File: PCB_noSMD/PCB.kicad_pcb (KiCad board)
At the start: 2 copper layers, 48.3 x 81.3 mm, 7 parts, among them J10 Screw_Terminal_01x02, J4 Conn_01x12_Socket, J5 Conn_01x16_Socket, J6 Conn_01x08_Socket, J7 Conn_01x06_Socket, J8 Conn_01x08_Socket, J9 Screw_Terminal_01x02

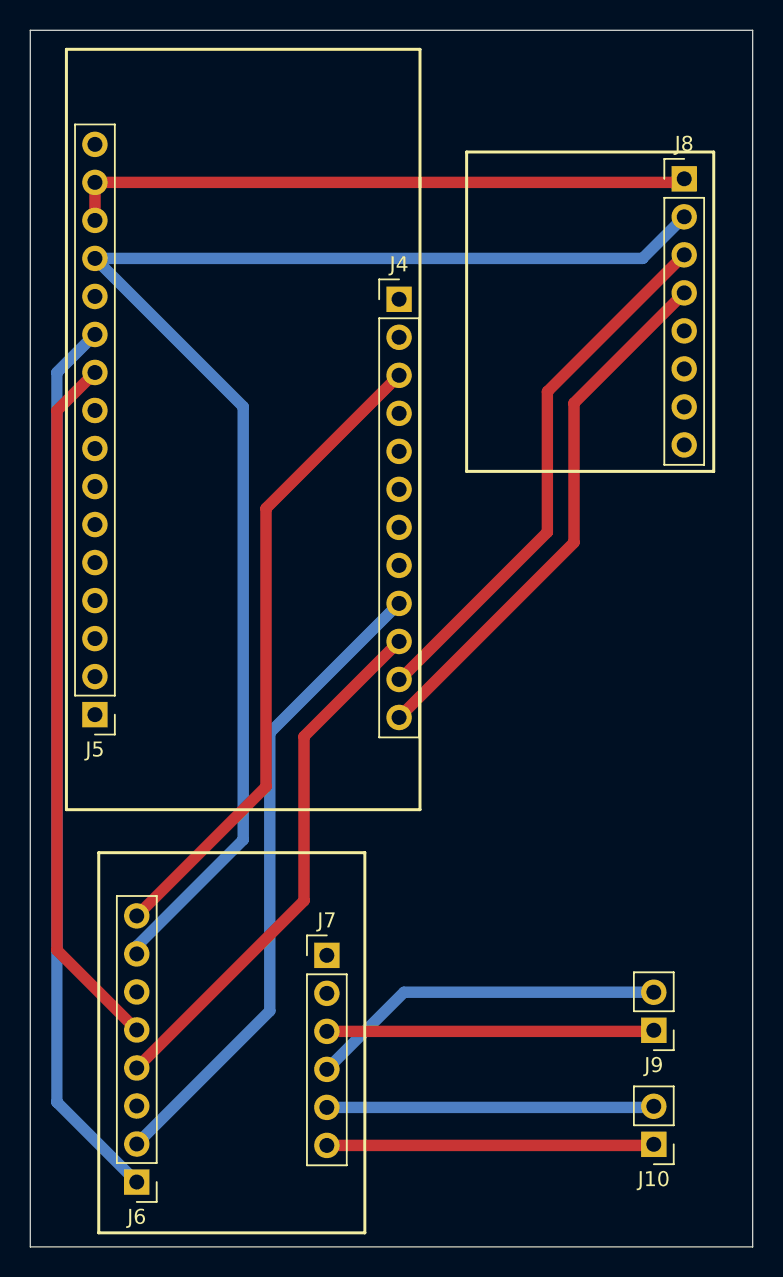
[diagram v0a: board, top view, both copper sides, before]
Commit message: Finished 2nd PCB
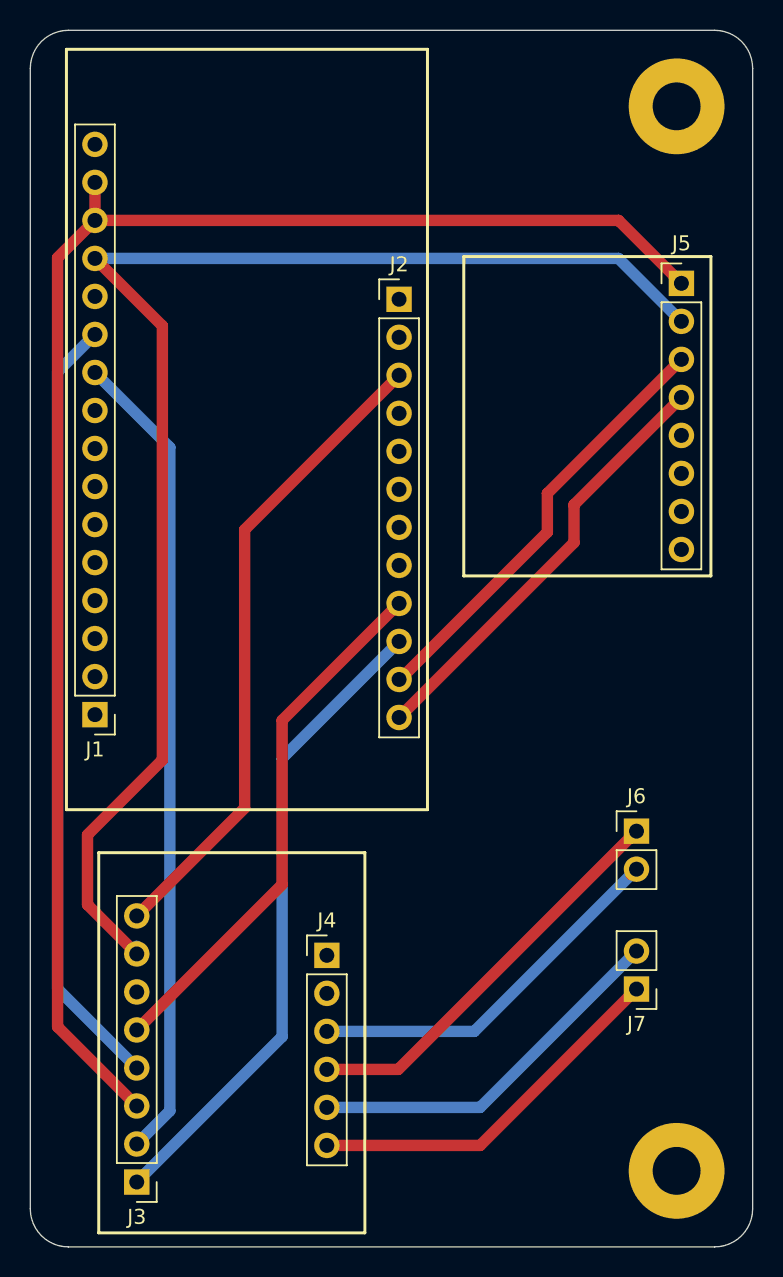
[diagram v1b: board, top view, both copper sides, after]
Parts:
- removed J10, J9: Screw_Terminal_01x02, Connector_PinHeader_2.54mm:PinHeader_1x02_P2.54mm_Vertical
- added J6: Screw_Terminal_01x02, Connector_PinHeader_2.54mm:PinHeader_1x02_P2.54mm_Vertical, F.Cu at (67.7, 85.3)
- added J7: Screw_Terminal_01x02, Connector_PinHeader_2.54mm:PinHeader_1x02_P2.54mm_Vertical, F.Cu at (67.7, 95.8)
- added REF**: MountingHole_3.2mm_M3_Pad, MountingHole:MountingHole_3.2mm_M3_Pad, F.Cu at (70.4, 108.0)
- added REF**: MountingHole_3.2mm_M3_Pad, MountingHole:MountingHole_3.2mm_M3_Pad, F.Cu at (70.4, 36.8)
- moved J5 6.99 mm to (70.7, 48.7)
- renumbered J5 to J1, J4 to J2, J6 to J3, J7 to J4, J8 to J5
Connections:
- J1 pad 10: BIN1 -> AIN2
- J1 pad 11: AIN1 -> BIN2
- J2 pad 10: BIN2 -> AIN1
- J2 pad 9: AIN2 -> BIN1
- J3 pad 3: unconnected-(J6-Pin_3-Pad3) -> +3.3V
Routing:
- net +3.3V: track 42.0 -> 106.2 mm
- net AIN1: track 59.9 -> 43.4 mm
- net BIN2: track 35.8 -> 52.2 mm
- net BIN1: track 47.2 -> 35.8 mm
- net AIN2: track 43.4 -> 54.5 mm
- net SDA: track 36.6 -> 29.2 mm
- net SCL: track 36.3 -> 29.2 mm
- net BOUT1: track 21.9 -> 25.7 mm
- net BOUT2: track 24.0 -> 27.3 mm
- net AOUT2: track 21.9 -> 25.0 mm
- net AOUT1: track 21.9 -> 25.0 mm
- net GND: track 94.0 -> 93.2 mm
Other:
- outline, holes or cut-outs redrawn
